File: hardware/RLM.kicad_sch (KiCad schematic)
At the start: 3 parts, among them U1 ESP32, U2 NRF24L01+, U3 MPU-6050

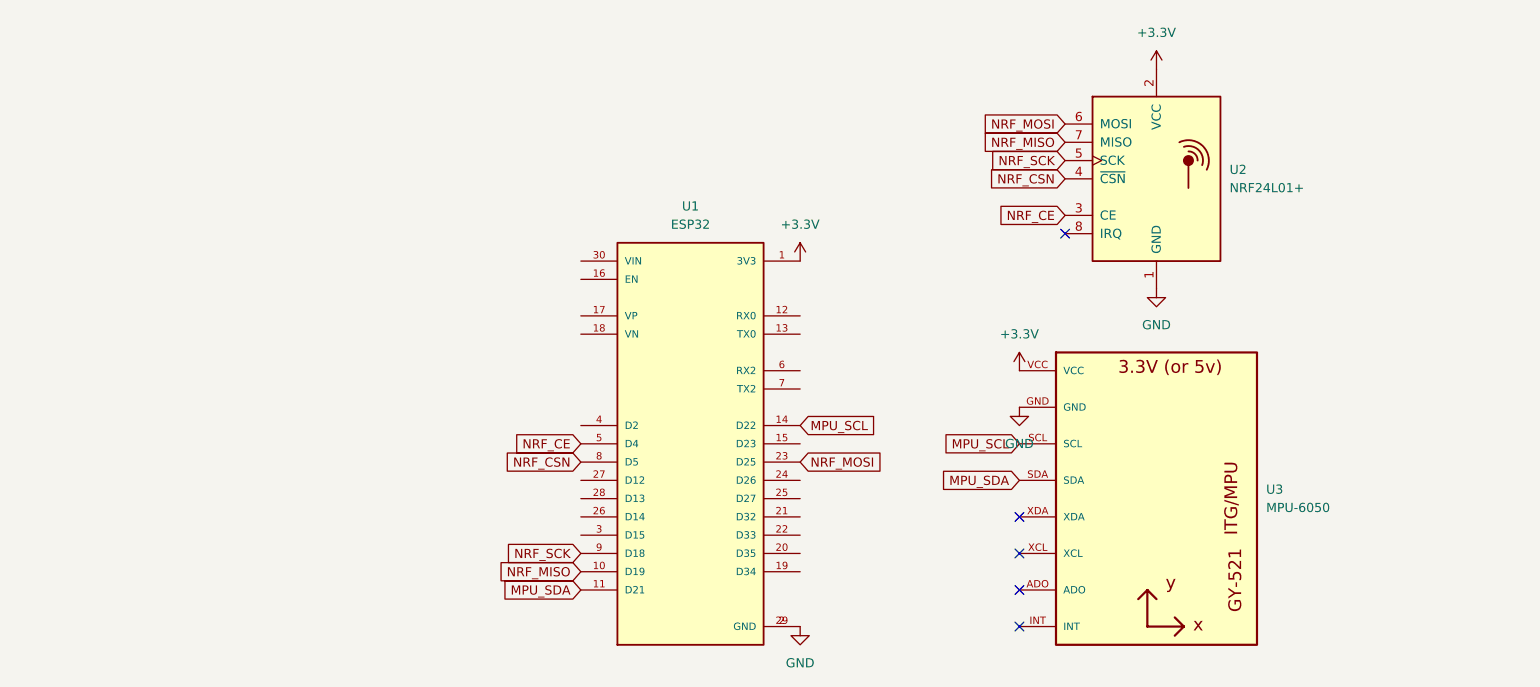
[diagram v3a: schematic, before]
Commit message: feat: add custom ESP32, NRF, GY modules
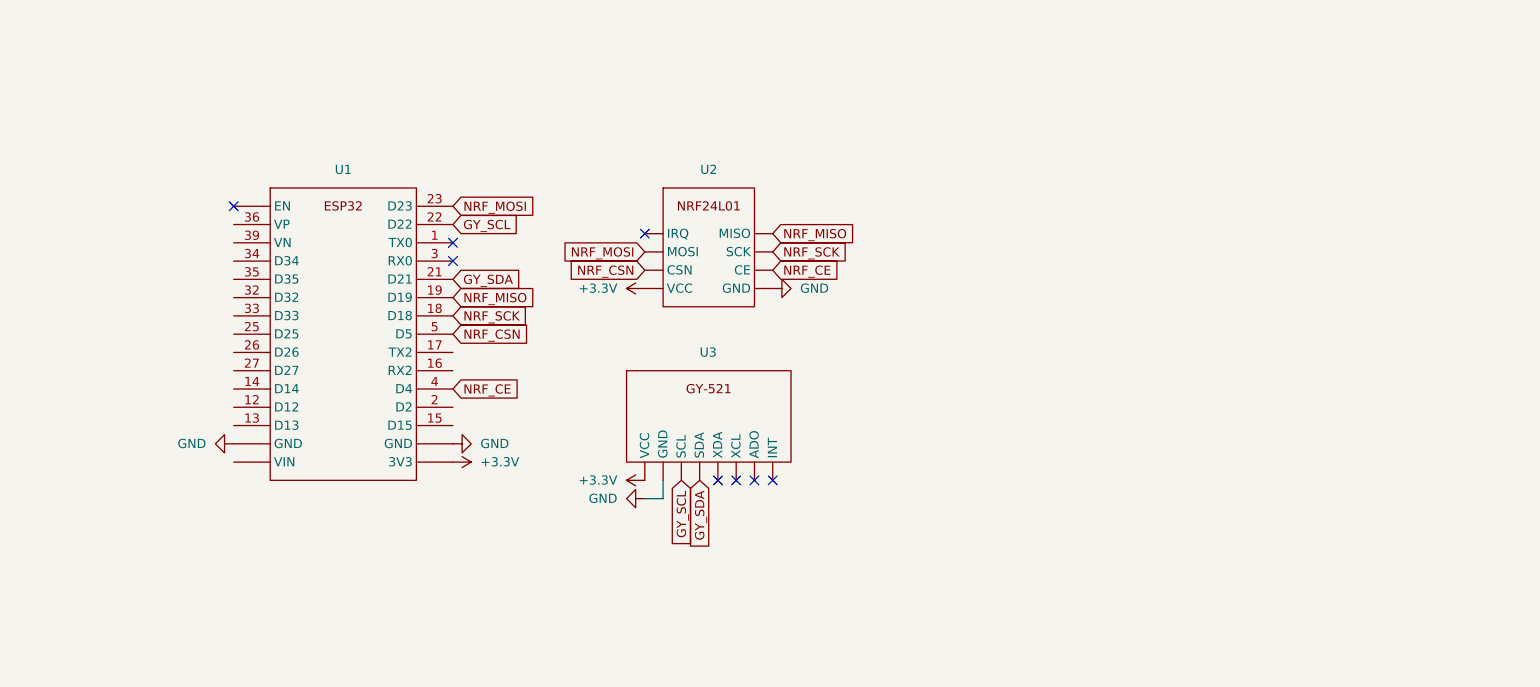
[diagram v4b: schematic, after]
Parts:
- removed U1: ESP32, GRC:MODULE_ESP32_DEVKIT_V1, symbol GRC_ESP32-DEVKIT-V1:ESP32-DEVKIT-V1
- removed U2: NRF24L01+, RF_Module:nRF24L01_Breakout, symbol RF:NRF24L01_Breakout
- removed U3: MPU-6050, GRC:GY-521, symbol GRC_GY-521:GY-521
- added U1: ~, symbol Remote-Logging-Module:ESP32
- added U2: ~, symbol Remote-Logging-Module:NRF24L01
- added U3: ~, symbol Remote-Logging-Module:GY-521
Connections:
- net +3.3V: now also U1. (VIN), U2. (VCC), U3. (XDA)
- net GND: now also U1. (VIN), U2. (VCC), U3. (XDA)
- net NRF_CE: now also U1.4 (D4), U2. (VCC)
- net NRF_CSN: now also U1.5 (D5), U2. (VCC)
- net NRF_MISO: now also U1.19 (D19), U2. (VCC)
- net NRF_MOSI: now also U1.23 (D23), U2. (VCC)
- net NRF_SCK: now also U1.18 (D18), U2. (VCC)
- new net GY_SCL: U1.22 (D22), U3. (XDA)
- new net GY_SDA: U1.21 (D21), U3. (XDA)
- no-connect marks 5 -> 8

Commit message: feat: add GPS and SD components
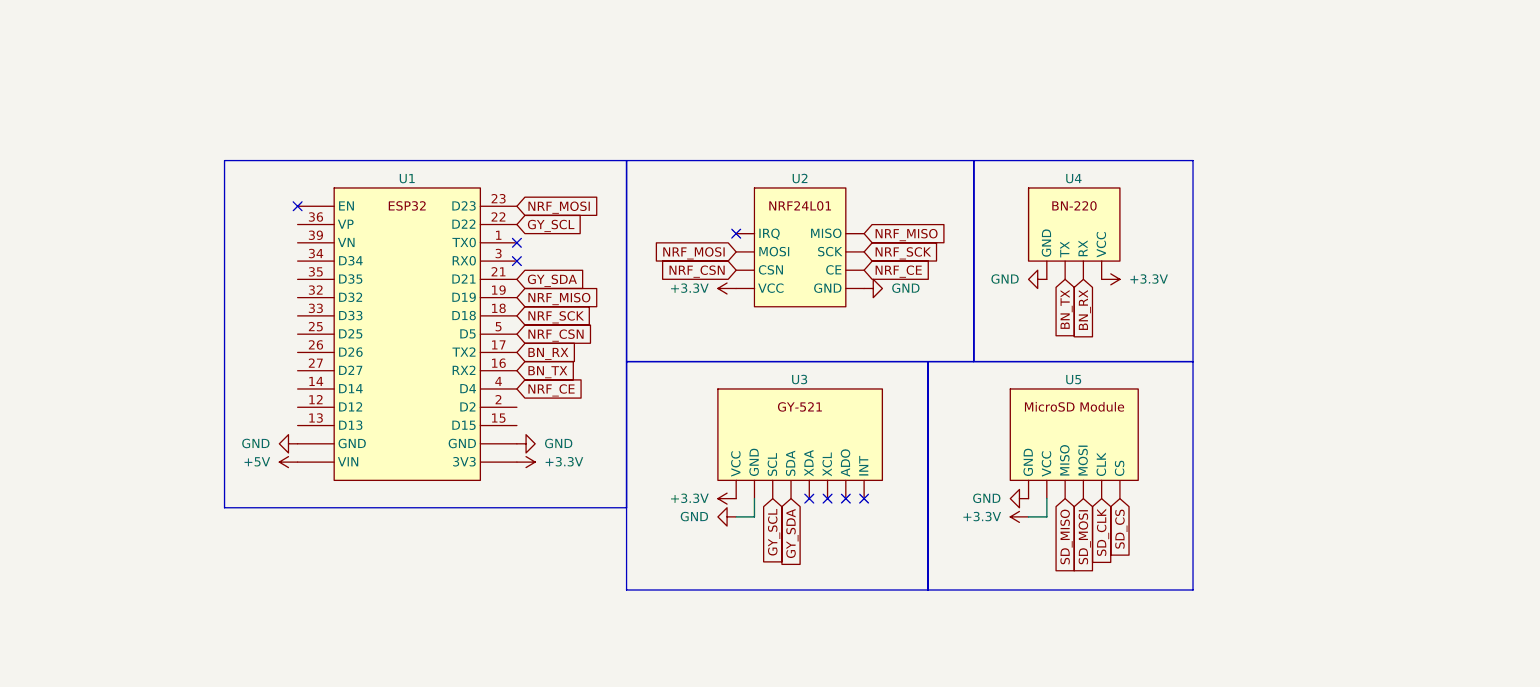
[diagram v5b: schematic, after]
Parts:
- removed U1: ~, symbol Remote-Logging-Module:ESP32
- removed U2: ~, symbol Remote-Logging-Module:NRF24L01
- removed U3: ~, symbol Remote-Logging-Module:GY-521
- added U1: ~, symbol GRC_Remote-Logging-Module:ESP32
- added U2: ~, symbol GRC_Remote-Logging-Module:NRF24L01
- added U3: ~, symbol GRC_Remote-Logging-Module:GY-521
- added U4: ~, symbol GRC_Remote-Logging-Module:BN-220
- added U5: ~, symbol GRC_Remote-Logging-Module:MicroSD-Module
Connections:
- net +3.3V: now also U1. (VIN), U2. (VCC), U3. (XDA), U4. (VCC), U5. (VCC)
- net GND: now also U1. (VIN), U2. (VCC), U3. (XDA), U4. (VCC), U5. (VCC)
- net GY_SCL: now also U1.22 (D22), U3. (XDA)
- net GY_SDA: now also U1.21 (D21), U3. (XDA)
- net NRF_CE: now also U1.4 (D4), U2. (VCC)
- net NRF_CSN: now also U1.5 (D5), U2. (VCC)
- net NRF_MISO: now also U1.19 (D19), U2. (VCC)
- net NRF_MOSI: now also U1.23 (D23), U2. (VCC)
- net NRF_SCK: now also U1.18 (D18), U2. (VCC)
- new net +5V: U1. (VIN)
- new net BN_RX: U1.17 (TX2), U4. (VCC)
- new net BN_TX: U1.16 (RX2), U4. (VCC)
- new net SD_CLK: U5. (VCC)
- new net SD_CS: U5. (VCC)
- new net SD_MISO: U5. (VCC)
- new net SD_MOSI: U5. (VCC)

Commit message: feat: add NRF adapter schematic
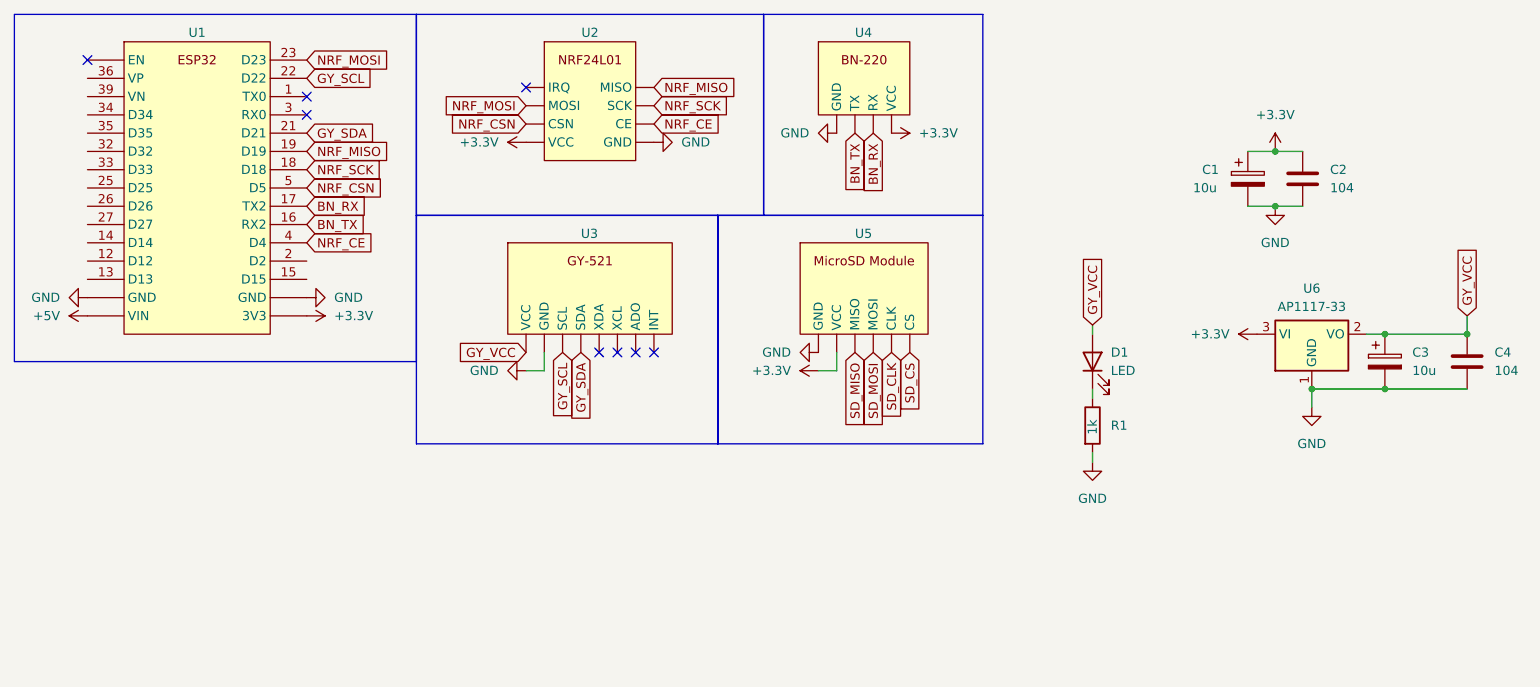
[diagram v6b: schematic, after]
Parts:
- added C1, C3: 10u, symbol Device:C_Polarized
- added C2, C4: 104, symbol Device:C
- added D1: LED, symbol Device:LED
- added R1: 1k, symbol Device:R
- added U6: AP1117-33, Package_TO_SOT_SMD:SOT-223-3_TabPin2, symbol Regulator_Linear:AP1117-33
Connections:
- net +3.3V: now also C1.1, C2.1, U6.3 (VI); no longer U3. (XDA)
- net GND: now also C1.2, C2.2, C3.2, C4.2, R1.2, U6.1 (GND)
- net GY_VCC: now reaches U3. (XDA)
- net GY_VCC: now also C3.1, C4.1, D1.2 (A), U6.2 (VO)
- new net: D1.1 (K), R1.1
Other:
- moved on the sheet: U1, U2, U3, U4, U5

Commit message: feat: add NRF adapter layout
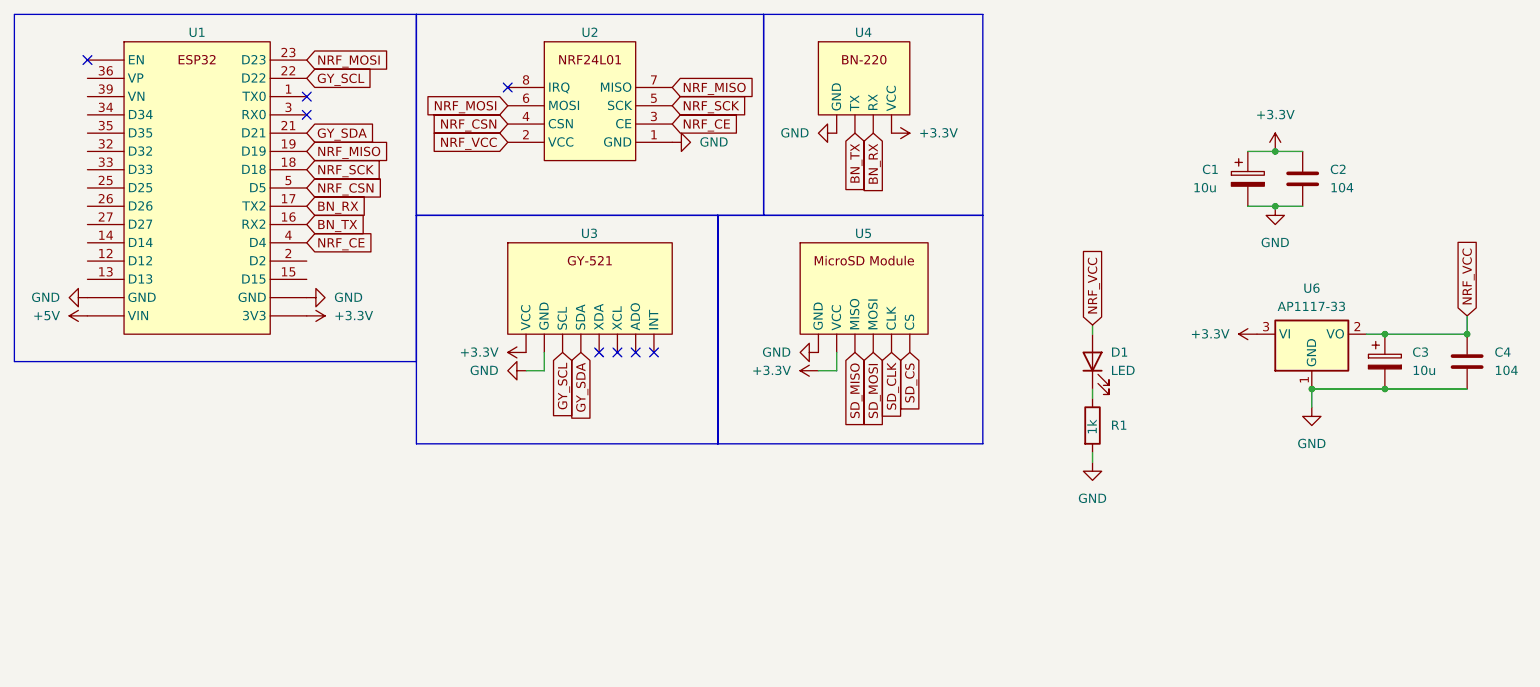
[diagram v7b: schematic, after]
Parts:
- C1, C2, C3, C4: footprint (none) -> Capacitor_SMD:C_0603_1608Metric_Pad1.08x0.95mm_HandSolder
- D1: footprint (none) -> LED_SMD:LED_0603_1608Metric_Pad1.05x0.95mm_HandSolder
- R1: footprint (none) -> Resistor_SMD:R_0603_1608Metric_Pad0.98x0.95mm_HandSolder
- U2: footprint (none) -> Connector_PinHeader_2.54mm:PinHeader_2x04_P2.54mm_Vertical
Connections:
- net +3.3V: now also U3. (XDA); no longer U2. (VCC)
- net GND: now also U2.1 (GND); no longer U2. (VCC)
- net NRF_CE: now also U2.3 (CE); no longer U2. (VCC)
- net NRF_CSN: now also U2.4 (CSN); no longer U2. (VCC)
- net NRF_MISO: now also U2.7 (MISO); no longer U2. (VCC)
- net NRF_MOSI: now also U2.6 (MOSI); no longer U2. (VCC)
- net NRF_SCK: now also U2.5 (SCK); no longer U2. (VCC)
- net GY_VCC renamed NRF_VCC
- net NRF_VCC: now also U2.2 (VCC); no longer U3. (XDA)

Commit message: feat: add ESP32, NRF, GY footprints
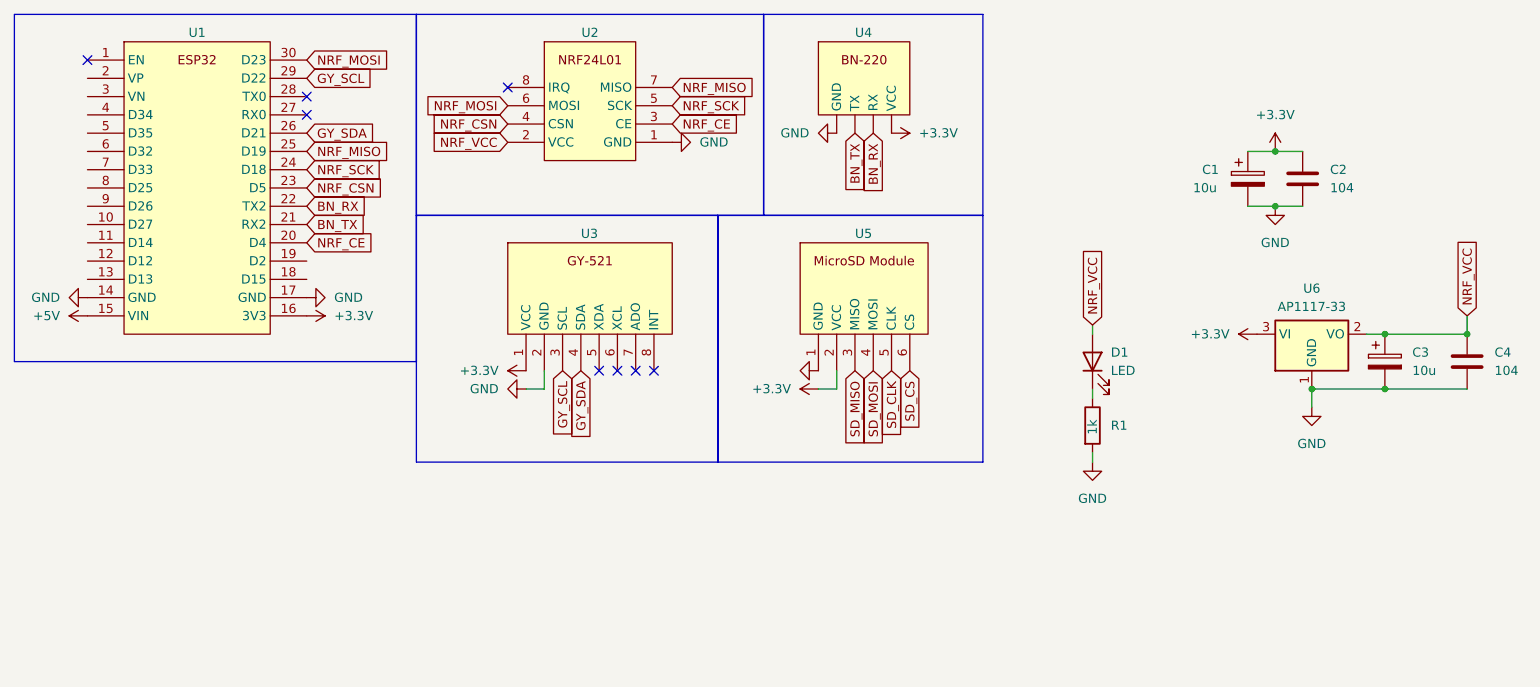
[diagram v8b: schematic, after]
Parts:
- U1: footprint (none) -> GRC:ESP32
- U2: footprint Connector_PinHeader_2.54mm:PinHeader_2x04_P2.54mm_Vertical -> GRC:NRF24L01
- U3: footprint (none) -> GRC:GY-521
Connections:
- net +3.3V: now also U1.16 (3V3), U3.1 (VCC), U5.2 (VCC); no longer U1. (VIN), U3. (XDA), U5. (VCC)
- net +5V: now also U1.15 (VIN); no longer U1. (VIN)
- net BN_RX: now also U1.22 (TX2); no longer U1.17 (TX2)
- net BN_TX: now also U1.21 (RX2); no longer U1.16 (RX2)
- net GND: now also U1.14 (GND), U1.17 (GND), U3.2 (GND), U5.1 (GND); no longer U1. (VIN), U3. (XDA), U5. (VCC)
- net GY_SCL: now also U1.29 (D22), U3.3 (SCL); no longer U1.22 (D22), U3. (XDA)
- net GY_SDA: now also U1.26 (D21), U3.4 (SDA); no longer U1.21 (D21), U3. (XDA)
- net NRF_CE: now also U1.20 (D4); no longer U1.4 (D4)
- net NRF_CSN: now also U1.23 (D5); no longer U1.5 (D5)
- net NRF_MISO: now also U1.25 (D19); no longer U1.19 (D19)
- net NRF_MOSI: now also U1.30 (D23); no longer U1.23 (D23)
- net NRF_SCK: now also U1.24 (D18); no longer U1.18 (D18)
- net SD_CLK: now also U5.5 (CLK); no longer U5. (VCC)
- net SD_CS: now also U5.6 (CS); no longer U5. (VCC)
- net SD_MISO: now also U5.3 (MISO); no longer U5. (VCC)
- net SD_MOSI: now also U5.4 (MOSI); no longer U5. (VCC)
